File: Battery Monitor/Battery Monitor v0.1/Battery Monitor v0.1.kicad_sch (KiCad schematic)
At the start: 27 parts, among them J1 XT60 M (Vertical), J2 Raspberry Pi 5, Q1 SUD50P10-43L, U1 15V-40V -> 12V 30A, U2 6-25V -> 5V 8A, U3 TLV1117-33IDCYR

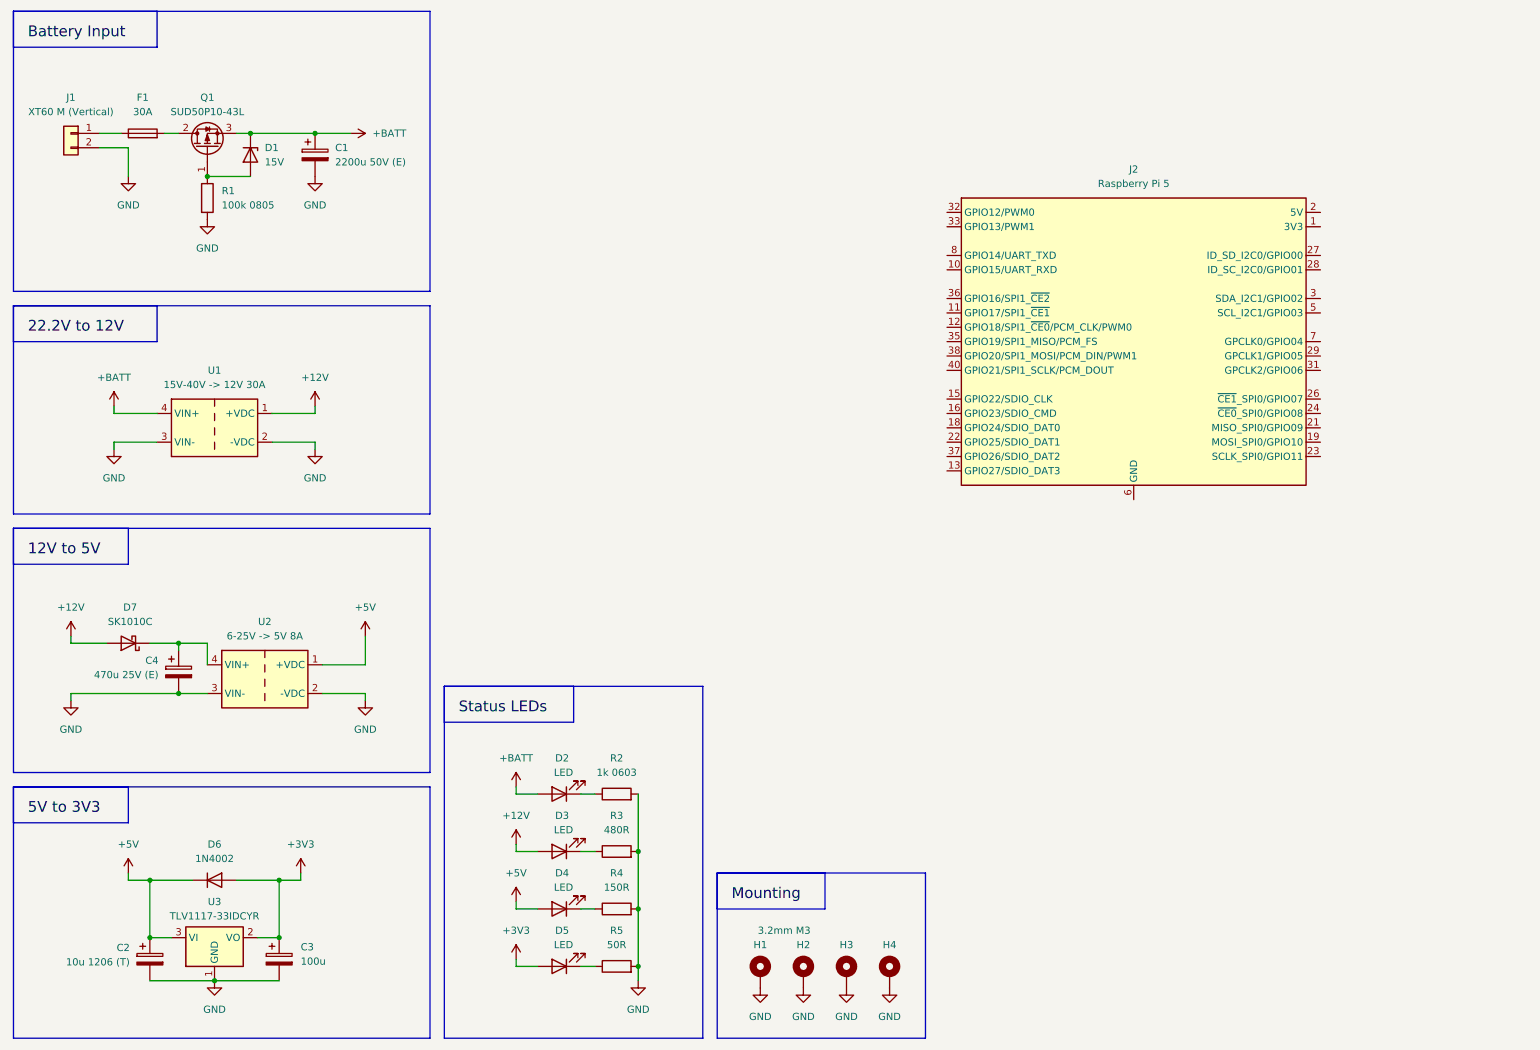
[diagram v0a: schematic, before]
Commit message: Began implementation of motor control & battery monitor
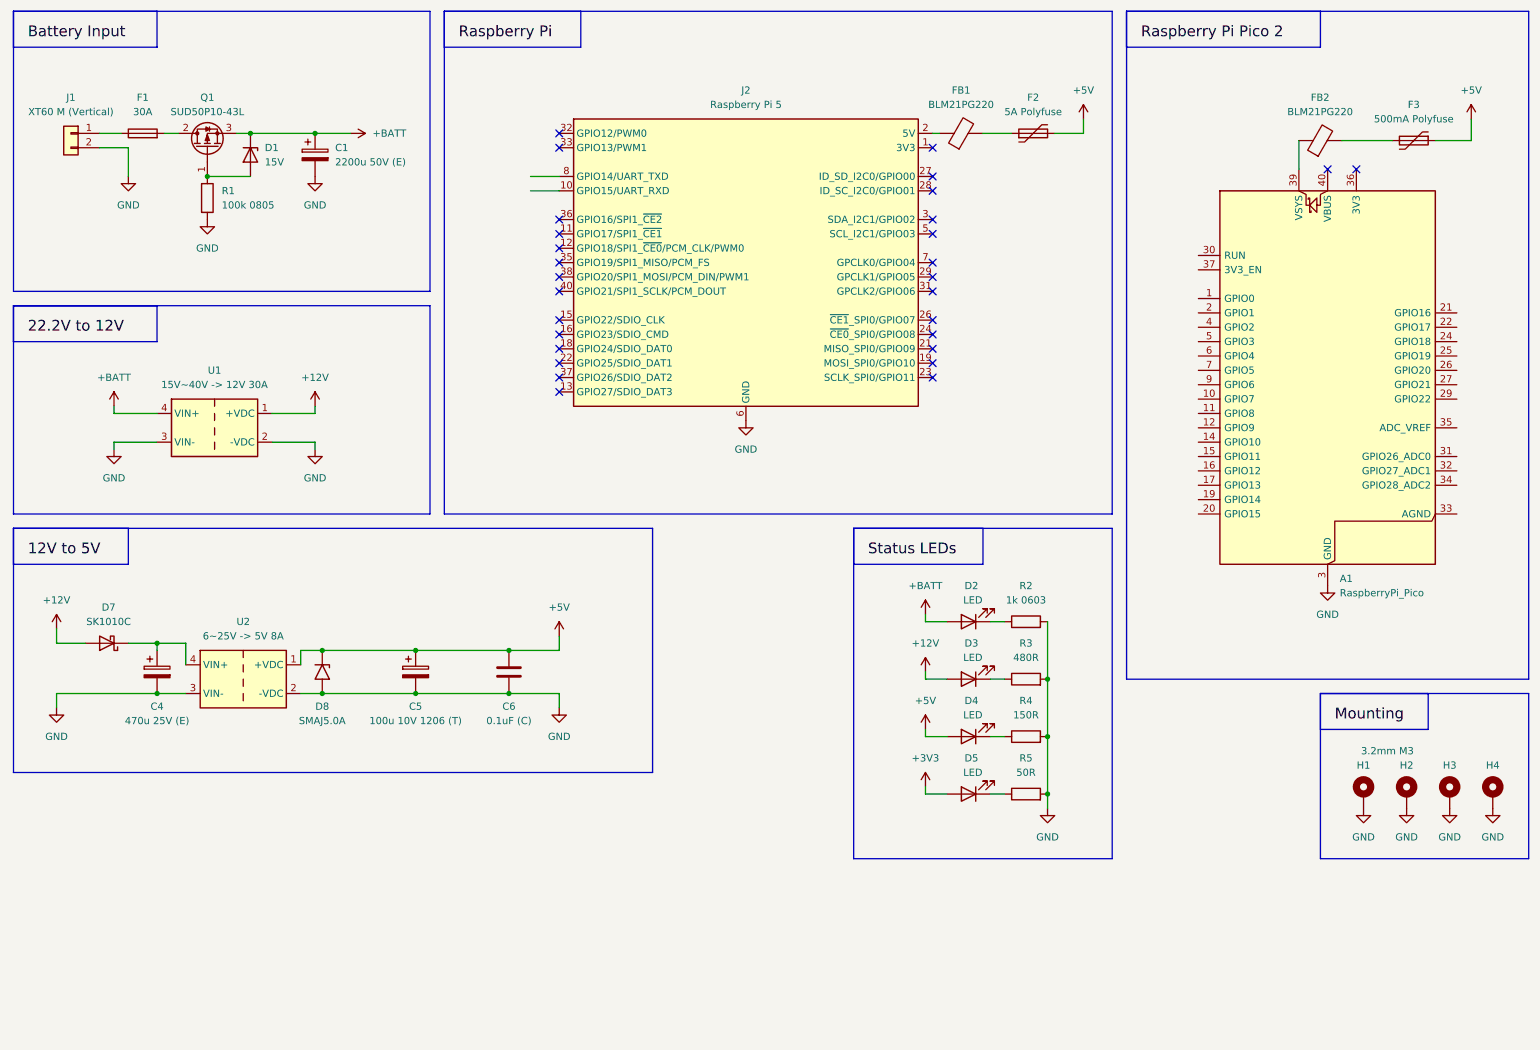
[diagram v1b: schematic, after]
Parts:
- removed C2: 10u 1206 (T), symbol Device:C_Polarized
- removed C3: 100u, symbol Device:C_Polarized
- removed D6: 1N4002, Diode_THT:D_DO-41_SOD81_P10.16mm_Horizontal, symbol Diode:1N4002
- removed U3: TLV1117-33IDCYR, Package_TO_SOT_SMD:SOT-223-3_TabPin2, symbol Regulator_Linear:LD1117S33TR_SOT223
- added A1: RaspberryPi_Pico, Module:RaspberryPi_Pico_Common_Unspecified, symbol MCU_Module:RaspberryPi_Pico
- added C5: 100u 10V 1206 (T), symbol Device:C_Polarized
- added C6: 0.1uF (C), symbol Device:C
- added D8: SMAJ5.0A, Diode_SMD:D_SMA, symbol Diode:SMAJ5.0A
- added F2: 5A Polyfuse, symbol Device:Polyfuse
- added F3: 500mA Polyfuse, symbol Device:Polyfuse
- added FB1, FB2: BLM21PG220, symbol Device:FerriteBead
- U1: value 15V-40V -> 12V 30A -> 15V~40V -> 12V 30A
- U2: value 6-25V -> 5V 8A -> 6~25V -> 5V 8A
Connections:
- net +5V: now also C5.1, C6.1, D8.1 (A1), F2.2, F3.1
- net GND: now also J2.14 (GND), J2.20 (GND), J2.25 (GND), J2.30 (GND), J2.34 (GND), J2.39 (GND), J2.6 (GND), J2.9 (GND), A1.13 (GND), A1.18 (GND), A1.23 (GND), A1.28 (GND), A1.3 (GND), A1.38 (GND), A1.8 (GND), C5.2, C6.2, D8.2 (A2)
- net at J2.2 (5V), J2.4 (5V): now also FB1.1
- new net: A1.39 (VSYS), FB2.1
- new net: F3.2, FB2.2
- new net: F2.1, FB1.2
- no-connect marks 0 -> 29
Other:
- moved on the sheet: C4, D2, D3, D4, D5, D7, H1, H2, H3, H4, J2, R2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
